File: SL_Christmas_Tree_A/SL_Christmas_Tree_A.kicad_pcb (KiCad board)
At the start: 2 copper layers, 85.7 x 133.1 mm, 60 parts, among them J101 GND, J102 5V, J201 GND, J202 5V

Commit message: PCB A v2.0
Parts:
- removed R101, R102, R103, R104, R105, R106, R107, R108, R109, R110, R111, R112, R201, R202, R203, R204, R205, R206, R207, R208, R209, R210, R211, R212: 200, Resistor_SMD:R_0805_2012Metric_Pad1.20x1.40mm_HandSolder
- added C101: 100nF, Capacitor_SMD:C_0805_2012Metric_Pad1.18x1.45mm_HandSolder, F.Cu at (82.0, 143.9)
- added C102: 100nF, Capacitor_SMD:C_0805_2012Metric_Pad1.18x1.45mm_HandSolder, F.Cu at (83.4, 133.4)
- added C103: 100nF, Capacitor_SMD:C_0805_2012Metric_Pad1.18x1.45mm_HandSolder, F.Cu at (88.3, 115.5)
- added C104: 100nF, Capacitor_SMD:C_0805_2012Metric_Pad1.18x1.45mm_HandSolder, F.Cu at (92.6, 103.5)
- added C105: 100nF, Capacitor_SMD:C_0805_2012Metric_Pad1.18x1.45mm_HandSolder, F.Cu at (94.0, 95.1)
- added C106: 100nF, Capacitor_SMD:C_0805_2012Metric_Pad1.18x1.45mm_HandSolder, F.Cu at (93.9, 78.5)
- added C107: 100nF, Capacitor_SMD:C_0805_2012Metric_Pad1.18x1.45mm_HandSolder, F.Cu at (101.9, 54.3)
- added C108: 100nF, Capacitor_SMD:C_0805_2012Metric_Pad1.18x1.45mm_HandSolder, F.Cu at (103.0, 84.2)
- added C109: 100nF, Capacitor_SMD:C_0805_2012Metric_Pad1.18x1.45mm_HandSolder, F.Cu at (106.8, 96.1)
- added C110: 100nF, Capacitor_SMD:C_0805_2012Metric_Pad1.18x1.45mm_HandSolder, F.Cu at (107.4, 105.0)
- added C111: 100nF, Capacitor_SMD:C_0805_2012Metric_Pad1.18x1.45mm_HandSolder, F.Cu at (112.1, 124.0)
- added C112: 100nF, Capacitor_SMD:C_0805_2012Metric_Pad1.18x1.45mm_HandSolder, F.Cu at (121.8, 138.1)
- added C113: 100nF, Capacitor_SMD:C_0805_2012Metric_Pad1.18x1.45mm_HandSolder, F.Cu at (107.2, 154.3)
- added C201: 100nF, Capacitor_SMD:C_0805_2012Metric_Pad1.18x1.45mm_HandSolder, B.Cu at (106.3, 156.8)
- added C202: 100nF, Capacitor_SMD:C_0805_2012Metric_Pad1.18x1.45mm_HandSolder, B.Cu at (117.4, 139.0)
- added C203: 100nF, Capacitor_SMD:C_0805_2012Metric_Pad1.18x1.45mm_HandSolder, B.Cu at (116.7, 128.2)
- added C204: 100nF, Capacitor_SMD:C_0805_2012Metric_Pad1.18x1.45mm_HandSolder, B.Cu at (109.3, 115.1)
- added C205: 100nF, Capacitor_SMD:C_0805_2012Metric_Pad1.18x1.45mm_HandSolder, B.Cu at (106.4, 102.3)
- added C206: 100nF, Capacitor_SMD:C_0805_2012Metric_Pad1.18x1.45mm_HandSolder, B.Cu at (105.2, 86.2)
- added C207: 100nF, Capacitor_SMD:C_0805_2012Metric_Pad1.18x1.45mm_HandSolder, B.Cu at (98.0, 54.5)
- added C208: 100nF, Capacitor_SMD:C_0805_2012Metric_Pad1.18x1.45mm_HandSolder, B.Cu at (102.0, 67.7)
- added C209: 100nF, Capacitor_SMD:C_0805_2012Metric_Pad1.18x1.45mm_HandSolder, B.Cu at (92.5, 79.7)
- added C210: 100nF, Capacitor_SMD:C_0805_2012Metric_Pad1.18x1.45mm_HandSolder, B.Cu at (92.7, 96.8)
- added C211: 100nF, Capacitor_SMD:C_0805_2012Metric_Pad1.18x1.45mm_HandSolder, B.Cu at (92.0, 118.5)
- added C212: 100nF, Capacitor_SMD:C_0805_2012Metric_Pad1.18x1.45mm_HandSolder, B.Cu at (87.0, 128.7)
- added C213: 100nF, Capacitor_SMD:C_0805_2012Metric_Pad1.18x1.45mm_HandSolder, B.Cu at (89.8, 151.8)
- added D113: SK6812MINI, parts:LED_SK6812MINI_PLCC4_3.5x3.5mm_P1.75mm, F.Cu at (114.2, 149.9)
- added D213: SK6812MINI, parts:LED_SK6812MINI_PLCC4_3.5x3.5mm_P1.75mm, B.Cu at (84.0, 144.8)
- added DIN101: TestPoint, TestPoint:TestPoint_Pad_3.0x3.0mm, F.Cu at (101.5, 61.9)
- added DIN202: TestPoint, TestPoint:TestPoint_Pad_3.0x3.0mm, B.Cu at (98.1, 61.8)
- added DOUT101: TestPoint, TestPoint:TestPoint_Pad_3.0x3.0mm, F.Cu at (98.1, 61.8)
- added DOUT201: TestPoint, TestPoint:TestPoint_Pad_3.0x3.0mm, B.Cu at (101.5, 61.9)
- added J103: DATA, Connector_Wire:SolderWire-1.5sqmm_1x01_D1.7mm_OD3.9mm, B.Cu at (91.6, 163.7)
- D101, D102, D103, D104, D105, D106, D108, D109, D110, D111, D112, D201, D202, D203, D204, D205, D206, D208, D209, D210, D211, D212: value LED -> SK6812MINI; footprint LED_SMD:LED_0807_Slow_Flashing_Diode -> parts:LED_SK6812MINI_PLCC4_3.5x3.5mm_P1.75mm
- D107, D207: value LED -> SK6812 4020; footprint LED_SMD:LED_0807_Slow_Flashing_Diode -> parts:LED_SK6812_4020
- moved D201 81.9 mm to (109.5, 148.8)
- moved D101 81.4 mm to (76.5, 146.8)
- moved D107 79.2 mm to (99.9, 49.0), turned to 180 degrees
- moved D207 79.2 mm to (99.8, 49.0), turned to 0 degrees
- moved D202 56.0 mm to (112.3, 134.6)
- moved D102 55.6 mm to (79.1, 127.8)
- moved D208 51.0 mm to (95.8, 66.3), turned to 0 degrees
- moved D111 47.6 mm to (117.8, 122.6), turned to 180 degrees
- moved D106 46.4 mm to (95.7, 67.0)
- moved D203 41.1 mm to (115.5, 122.9)
- moved D209 40.3 mm to (91.7, 89.2), turned to 0 degrees
- moved D206 40.0 mm to (107.0, 80.7)
- moved D210 39.5 mm to (86.6, 101.5), turned to 0 degrees
- moved D212 37.9 mm to (80.2, 125.3), turned to 0 degrees
- moved D108 37.0 mm to (107.1, 78.6), turned to 180 degrees
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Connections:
- D101 pad 1: GND -> Net-(D101-DOUT)
- D101 pad 2: Net-(D101-Pad2) -> GND
- D101 pad 3: (no net) -> Net-(D101-DIN)
- D101 pad 4: (no net) -> +5V
- D102 pad 1: GND -> Net-(D102-DOUT)
- D102 pad 2: Net-(D102-Pad2) -> GND
- D102 pad 3: (no net) -> Net-(D101-DOUT)
- D102 pad 4: (no net) -> +5V
- D103 pad 1: GND -> Net-(D103-DOUT)
- D103 pad 2: Net-(D103-Pad2) -> GND
- D103 pad 3: (no net) -> Net-(D102-DOUT)
- D103 pad 4: (no net) -> +5V
- D104 pad 1: GND -> Net-(D104-DOUT)
- D104 pad 2: Net-(D104-Pad2) -> GND
- D104 pad 3: (no net) -> Net-(D103-DOUT)
- D104 pad 4: (no net) -> +5V
- D105 pad 1: GND -> Net-(D105-DOUT)
- D105 pad 2: Net-(D105-Pad2) -> GND
- D105 pad 3: (no net) -> Net-(D104-DOUT)
- D105 pad 4: (no net) -> +5V
- D106 pad 1: GND -> Net-(D106-DOUT)
- D106 pad 2: Net-(D106-Pad2) -> GND
- D106 pad 3: (no net) -> Net-(D105-DOUT)
- D106 pad 4: (no net) -> +5V
- D107 pad 1: GND -> Net-(D106-DOUT)
- D107 pad 2: Net-(D107-Pad2) -> +5V
- D107 pad 3: (no net) -> Net-(D107-DOUT)
- D107 pad 4: (no net) -> GND
- D108 pad 1: GND -> Net-(D108-DOUT)
- D108 pad 2: Net-(D108-Pad2) -> GND
- D108 pad 3: (no net) -> Net-(D108-DIN)
- D108 pad 4: (no net) -> +5V
- D109 pad 1: GND -> Net-(D109-DOUT)
- D109 pad 2: Net-(D109-Pad2) -> GND
- D109 pad 3: (no net) -> Net-(D108-DOUT)
- D109 pad 4: (no net) -> +5V
- D110 pad 1: GND -> Net-(D110-DOUT)
- D110 pad 2: Net-(D110-Pad2) -> GND
- D110 pad 3: (no net) -> Net-(D109-DOUT)
- D110 pad 4: (no net) -> +5V
- D111 pad 1: GND -> Net-(D111-DOUT)
- D111 pad 2: Net-(D111-Pad2) -> GND
- D111 pad 3: (no net) -> Net-(D110-DOUT)
- D111 pad 4: (no net) -> +5V
- D112 pad 1: GND -> Net-(D112-DOUT)
- D112 pad 2: Net-(D112-Pad2) -> GND
- D112 pad 3: (no net) -> Net-(D111-DOUT)
- D112 pad 4: (no net) -> +5V
- D201 pad 1: GND -> Net-(D201-DOUT)
- D201 pad 2: Net-(D201-Pad2) -> GND
- D201 pad 3: (no net) -> Conn_A-OUT_B-IN
- D201 pad 4: (no net) -> +5V
- D202 pad 1: GND -> Net-(D202-DOUT)
- D202 pad 2: Net-(D202-Pad2) -> GND
- D202 pad 3: (no net) -> Net-(D201-DOUT)
- D202 pad 4: (no net) -> +5V
- D203 pad 1: GND -> Net-(D203-DOUT)
- D203 pad 2: Net-(D203-Pad2) -> GND
- D203 pad 3: (no net) -> Net-(D202-DOUT)
- D203 pad 4: (no net) -> +5V
- D204 pad 1: GND -> Net-(D204-DOUT)
- D204 pad 2: Net-(D204-Pad2) -> GND
- D204 pad 3: (no net) -> Net-(D203-DOUT)
- D204 pad 4: (no net) -> +5V
- D205 pad 1: GND -> Net-(D205-DOUT)
- D205 pad 2: Net-(D205-Pad2) -> GND
- D205 pad 3: (no net) -> Net-(D204-DOUT)
- D205 pad 4: (no net) -> +5V
- D206 pad 1: GND -> Net-(D206-DOUT)
- D206 pad 2: Net-(D206-Pad2) -> GND
- D206 pad 3: (no net) -> Net-(D205-DOUT)
- D206 pad 4: (no net) -> +5V
- D207 pad 1: GND -> Net-(D206-DOUT)
- D207 pad 2: Net-(D207-Pad2) -> +5V
- D207 pad 3: (no net) -> Net-(D207-DOUT)
- D207 pad 4: (no net) -> GND
- D208 pad 1: GND -> Net-(D208-DOUT)
- D208 pad 2: Net-(D208-Pad2) -> GND
- D208 pad 3: (no net) -> Net-(D208-DIN)
- D208 pad 4: (no net) -> +5V
- D209 pad 1: GND -> Net-(D209-DOUT)
- D209 pad 2: Net-(D209-Pad2) -> GND
- D209 pad 3: (no net) -> Net-(D208-DOUT)
- D209 pad 4: (no net) -> +5V
- D210 pad 1: GND -> Net-(D210-DOUT)
- D210 pad 2: Net-(D210-Pad2) -> GND
- D210 pad 3: (no net) -> Net-(D209-DOUT)
- D210 pad 4: (no net) -> +5V
- D211 pad 1: GND -> Net-(D211-DOUT)
- D211 pad 2: Net-(D211-Pad2) -> GND
- D211 pad 3: (no net) -> Net-(D210-DOUT)
- D211 pad 4: (no net) -> +5V
- D212 pad 1: GND -> Net-(D212-DOUT)
- D212 pad 2: Net-(D212-Pad2) -> GND
- D212 pad 3: (no net) -> Net-(D211-DOUT)
- D212 pad 4: (no net) -> +5V
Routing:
- net GND: track 2.47 -> 1198.7 mm, vias 57 -> 105
- net +5V: track 503.8 -> 681.9 mm, vias 8 -> 12
- net Net-(D206-DOUT): track 0.00 -> 39.0 mm
- net Net-(D101-DIN): track 0.00 -> 24.4 mm
- net Net-(D106-DOUT): track 0.00 -> 23.8 mm
- net Net-(D208-DOUT): track 0.00 -> 23.5 mm
- net Net-(D109-DOUT): track 0.00 -> 23.1 mm
- net Net-(D105-DOUT): track 0.00 -> 22.6 mm
- net Net-(D212-DOUT): track 0.00 -> 20.7 mm
- net Net-(D101-DOUT): track 0.00 -> 20.7 mm
- net Net-(D102-DOUT): track 0.00 -> 18.7 mm
- net Net-(D108-DIN): track 0.00 -> 17.9 mm
- net Net-(D111-DOUT): track 0.00 -> 16.3 mm
- net Net-(D203-DOUT): track 0.00 -> 15.7 mm
- net Net-(D205-DOUT): track 0.00 -> 15.5 mm
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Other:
- outline, holes or cut-outs redrawn
- board text added: "D"
- board text added: "DATA"

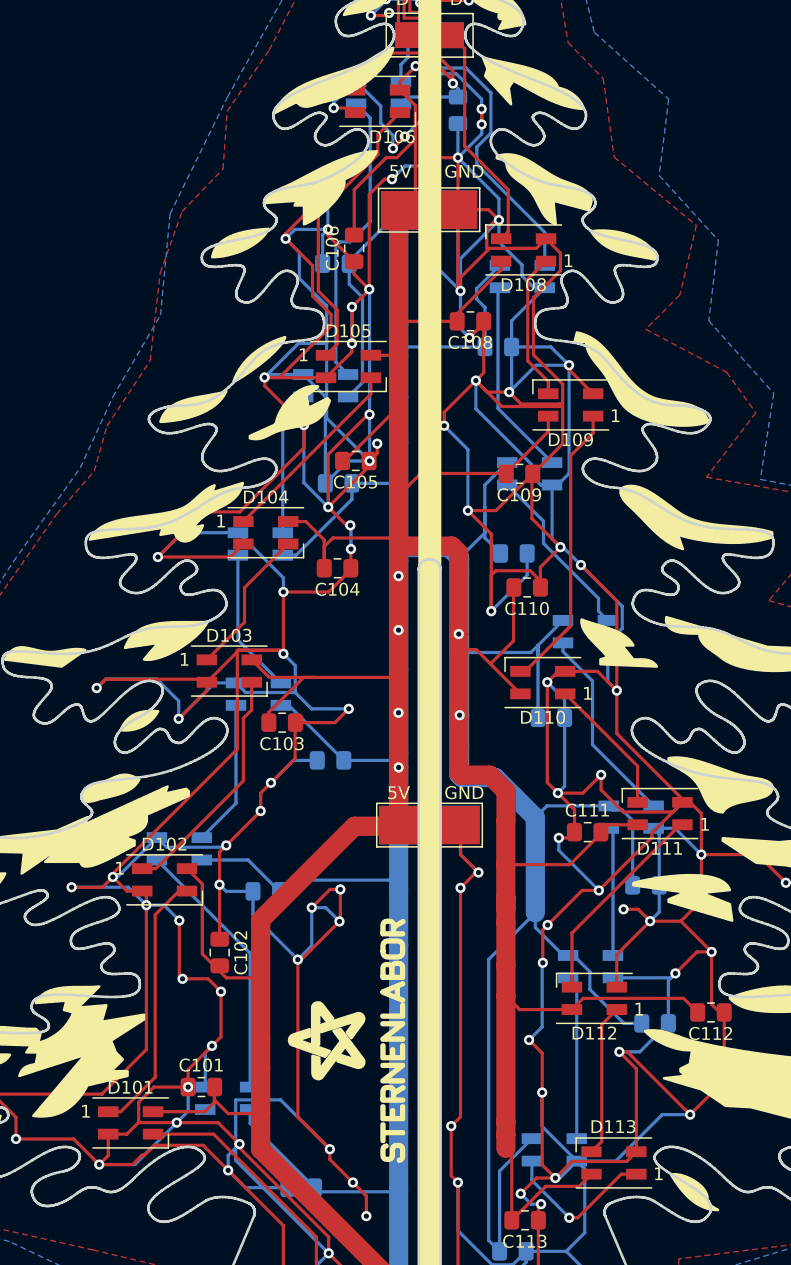
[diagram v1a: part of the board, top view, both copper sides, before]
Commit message: small Footprint changes and prepared "Side B" for placing parts
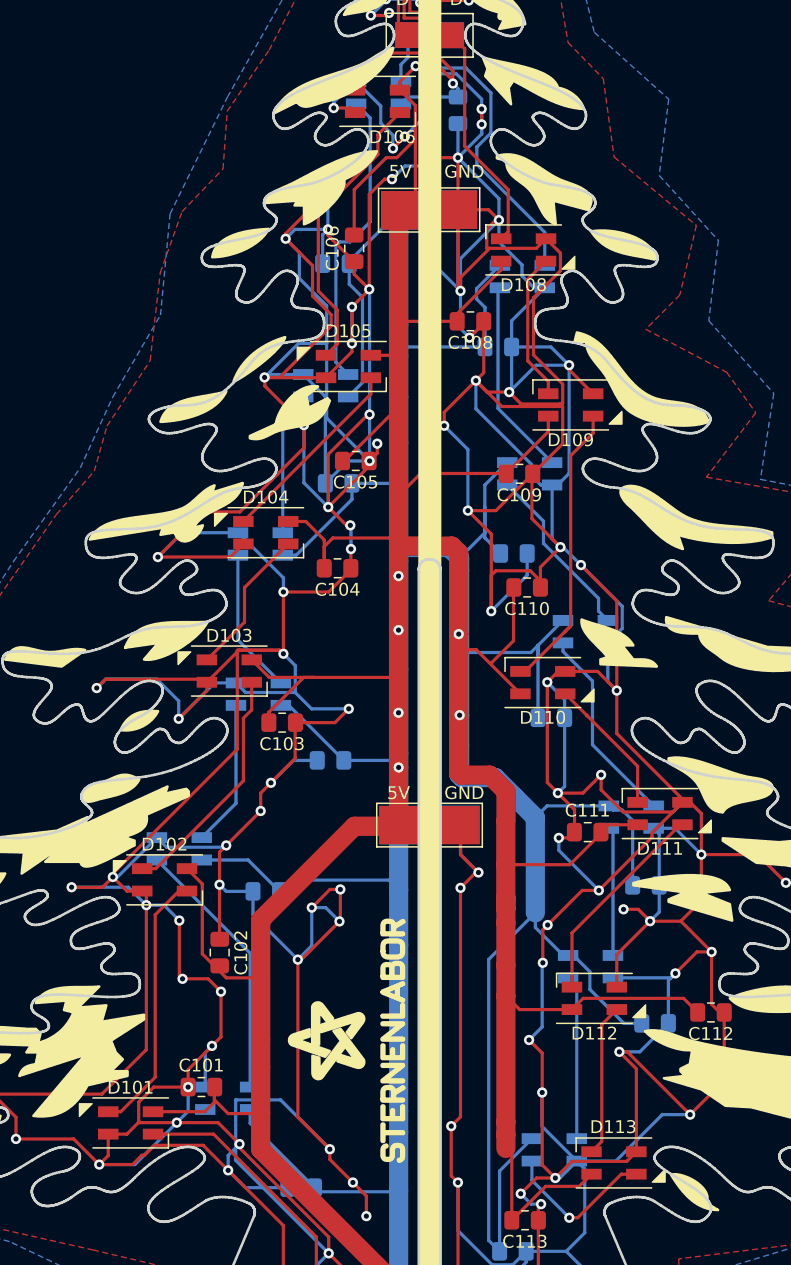
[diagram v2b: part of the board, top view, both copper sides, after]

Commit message: WIP v2.1
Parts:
- added DS: DS, Connector_Wire:SolderWire-1.5sqmm_1x01_D1.7mm_OD3.9mm, F.Cu at (108.0, 163.7)
- J103: value DATA -> DT
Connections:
- D107 pad 1: Net-(D106-DOUT) -> Net-(D107-DIN)
- D207 pad 1: Net-(D206-DOUT) -> Net-(D107-DOUT)
- D207 pad 3: Net-(D207-DOUT) -> Net-(D107-DIN)
- DOUT101 pad 1: Net-(D107-DOUT) -> Net-(D106-DOUT)
- DOUT201 pad 1: Net-(D207-DOUT) -> Net-(D107-DIN)
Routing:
- net Net-(D107-DIN): track 0.00 -> 148.5 mm, vias 0 -> 9
- net Net-(D206-DOUT): track 39.0 -> 0.00 mm
- net Net-(D106-DOUT): track 23.8 -> 7.73 mm
- net Net-(D207-DOUT): track 14.7 -> 0.00 mm
- net Net-(D107-DOUT): track 13.5 -> 5.70 mm, vias 0 -> 1
- net +5V: track 681.9 -> 682.7 mm
- net GND: track 1198.7 -> 1198.9 mm, vias 105 -> 110
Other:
- board text added: "DS"
- board text added: "DT"
- board text removed: "D"
- board text removed: "DATA"

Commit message: v2.1 Final
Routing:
- net GND: vias 110 -> 116
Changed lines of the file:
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@@
 	(title_block
 		(title "Christmas Tree 2024 - Side A")
-		(date "2024-10-15")
+		(date "2024-11-01")
 		(rev "2.1")
 		(company "Sternenlabor e.V.")
@@
 	)
 	(via
+		(at 106.69 119.225)
+		(size 0.8)
+		(drill 0.4)
+		(layers "F.Cu" "B.Cu")
+		(free yes)
+		(net 2)
+	)
+	(via
 		(at 80.5 135.5)
 		(size 0.8)
@@
 	)
 	(via
+		(at 101.75 87.525)
+		(size 0.8)
+		(drill 0.4)
+		(layers "F.Cu" "B.Cu")
+		(free yes)
+		(net 2)
+	)
+	(via
 		(at 121.8 133.4)
 		(size 0.8)
@@
 	)
 	(via
+		(at 107.15 109.825)
+		(size 0.8)
+		(drill 0.4)
+		(layers "F.Cu" "B.Cu")
+		(free yes)
+		(net 2)
+	)
+	(via
 		(at 102.9 85.45)
 		(size 0.8)
@@
 	)
 	(via
+		(at 104.15 131.3)
+		(size 0.8)
+		(drill 0.4)
+		(layers "F.Cu" "B.Cu")
+		(free yes)
+		(net 2)
+	)
+	(via
 		(at 110 101.8)
 		(size 0.8)
@@
 	)
 	(via
+		(at 105.225 113.45)
+		(size 0.8)
+		(drill 0.4)
+		(layers "F.Cu" "B.Cu")
+		(free yes)
+		(net 2)
+	)
+	(via
 		(at 93.475 114.425)
 		(size 0.8)
@@
 		(net 2)
 	)
+	(via
+		(at 105.5 117.85)
+		(size 0.8)
+		(drill 0.4)
+		(layers "F.Cu" "B.Cu")
+		(free yes)
+		(net 2)
+	)

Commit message: Fix routing issues on PCB A
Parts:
- renumbered DS to J2
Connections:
- D207 pad 3: Net-(D107-DIN) -> unconnected-(D207-DOUT-Pad3)
- DOUT201 pad 1: Net-(D107-DIN) -> Net-(D206-DOUT)
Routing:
- net Net-(D206-DOUT): track 0.00 -> 21.9 mm
- net Net-(D107-DIN): track 148.5 -> 134.2 mm
- net GND: track 1198.9 -> 1196.8 mm, vias 116 -> 118
